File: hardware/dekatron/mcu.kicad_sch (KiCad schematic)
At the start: 30 parts, among them J301 DISP, J302 NIX_LV, U301 RP2040-Zero

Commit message: Tie the dekatron cathodes at the socket; add Phase 1C PCB tooling (WIP)
Cathodes K0, K2-K9 are joined at the socket and return on one RTN wire, as
in the AD01 reference: LK6-LK14 and J203 removed, tube harness is anode
(J201) + G1, G2, K1, RTN (J202, 4 pads). Netlist diff: only the nine
TUBE_Kn nets and the RTN link pins change. ERC 1 (intentional).

Also adds work-in-progress PCB tooling: gen_pcb.py (pcbnew placement,
outline, pours, rules), route_pcb.py (class-aware A* router adapted from
nanovolt-divider), pcb_io.py, and dekatron.kicad_dru with the corrected
HV pair rules (HV to HV/VB/HVSTR 1.5 mm, to bias/logic 3.0 mm). Harness
landings use plain wire pads with cable-tie anchors. The board itself is
not committed yet: placement is being reworked.

Co-Authored-By: Claude Opus 5.5 <noreply@anthropic.com>
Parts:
- J301: footprint Connector_Wire:SolderWire-0.5sqmm_1x05_P4.8mm_D0.9mm_OD2.3mm_Relief -> Connector_Wire:SolderWire-0.5sqmm_1x05_P4.8mm_D0.9mm_OD2.3mm
- J302: footprint Connector_Wire:SolderWire-0.5sqmm_1x06_P4.8mm_D0.9mm_OD2.3mm_Relief -> Connector_Wire:SolderWire-0.5sqmm_1x06_P4.8mm_D0.9mm_OD2.3mm
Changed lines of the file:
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@@
 	  (property "Reference" "J301" (at 153.06 242.84 0) (show_name no) (do_not_autoplace no) (effects (font (size 1.27 1.27)) (justify left)))
 	  (property "Value" "DISP" (at 153.06 245.44 0) (show_name no) (do_not_autoplace no) (effects (font (size 1.27 1.27)) (justify left)))
-	  (property "Footprint" "Connector_Wire:SolderWire-0.5sqmm_1x05_P4.8mm_D0.9mm_OD2.3mm_Relief" (at 149.86 243.84 0) (hide yes) (show_name no) (do_not_autoplace no) (effects (font (size 1.27 1.27)) (justify left)))
+	  (property "Footprint" "Connector_Wire:SolderWire-0.5sqmm_1x05_P4.8mm_D0.9mm_OD2.3mm" (at 149.86 243.84 0) (hide yes) (show_name no) (do_not_autoplace no) (effects (font (size 1.27 1.27)) (justify left)))
 	  (property "Datasheet" "" (at 149.86 243.84 0) (hide yes) (show_name no) (do_not_autoplace no) (effects (font (size 1.27 1.27)) (justify left)))
 	  (property "Description" "Generic connector, single row, 01x05, script generated (kicad-library-utils/schlib/autogen/connector/)" (at 149.86 243.84 0) (hide yes) (show_name no) (do_not_autoplace no) (effects (font (size 1.27 1.27)) (justify left)))
@@
 	  (property "Reference" "J302" (at 214.02 242.84 0) (show_name no) (do_not_autoplace no) (effects (font (size 1.27 1.27)) (justify left)))
 	  (property "Value" "NIX_LV" (at 214.02 245.44 0) (show_name no) (do_not_autoplace no) (effects (font (size 1.27 1.27)) (justify left)))
-	  (property "Footprint" "Connector_Wire:SolderWire-0.5sqmm_1x06_P4.8mm_D0.9mm_OD2.3mm_Relief" (at 210.82 243.84 0) (hide yes) (show_name no) (do_not_autoplace no) (effects (font (size 1.27 1.27)) (justify left)))
+	  (property "Footprint" "Connector_Wire:SolderWire-0.5sqmm_1x06_P4.8mm_D0.9mm_OD2.3mm" (at 210.82 243.84 0) (hide yes) (show_name no) (do_not_autoplace no) (effects (font (size 1.27 1.27)) (justify left)))
 	  (property "Datasheet" "" (at 210.82 243.84 0) (hide yes) (show_name no) (do_not_autoplace no) (effects (font (size 1.27 1.27)) (justify left)))
 	  (property "Description" "Generic connector, single row, 01x06, script generated (kicad-library-utils/schlib/autogen/connector/)" (at 210.82 243.84 0) (hide yes) (show_name no) (do_not_autoplace no) (effects (font (size 1.27 1.27)) (justify left)))

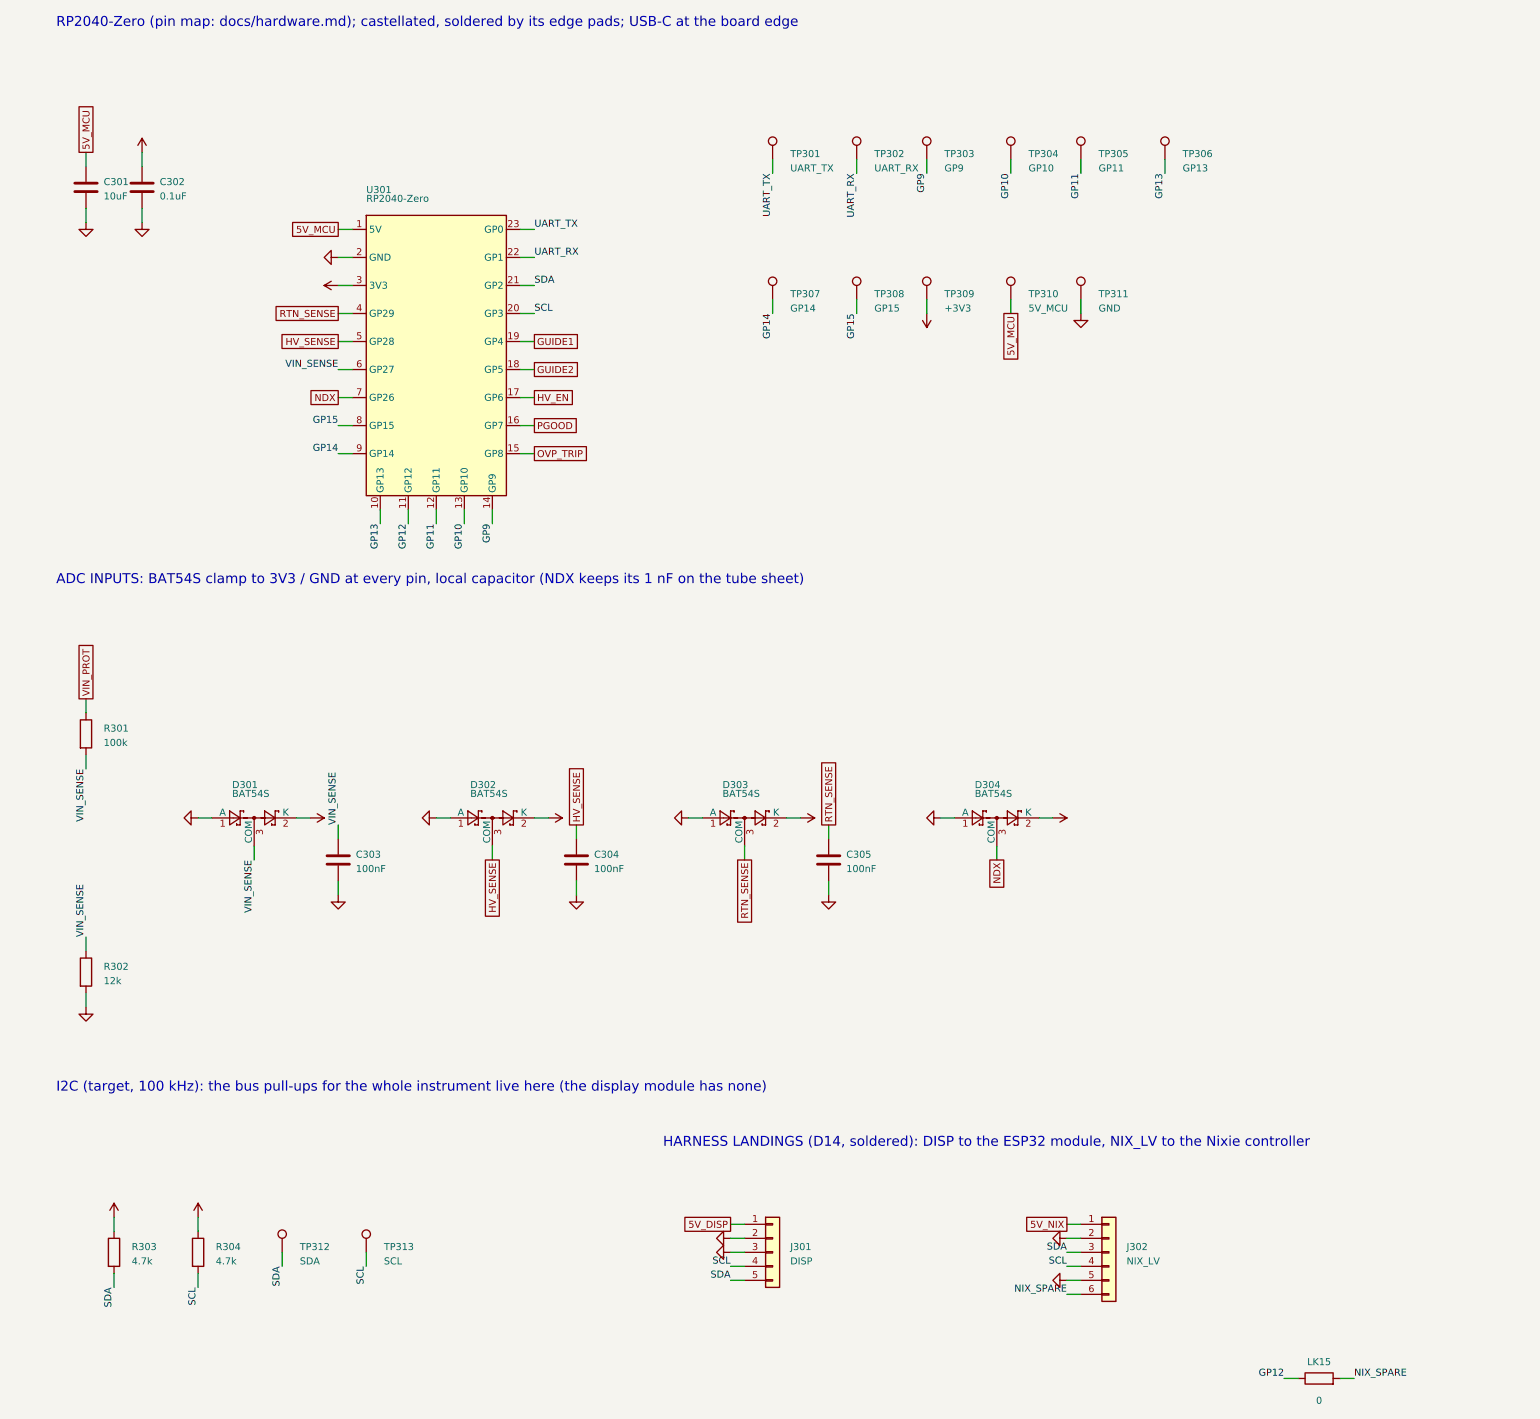
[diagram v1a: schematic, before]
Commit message: Redraw the dekatron schematics as wired, readable sheets
Each block is now drawn with real wires, power/GND symbols and junctions
instead of per-pin label stubs. Net names used by the PCB scripts and net
classes are kept as local labels; inter-sheet nets stay global labels.
Netlist pin partition verified identical to the previous version; ERC
unchanged (1 intentional LP2951/LM5156 power-output violation).

Co-Authored-By: Claude Opus 5.5 <noreply@anthropic.com>
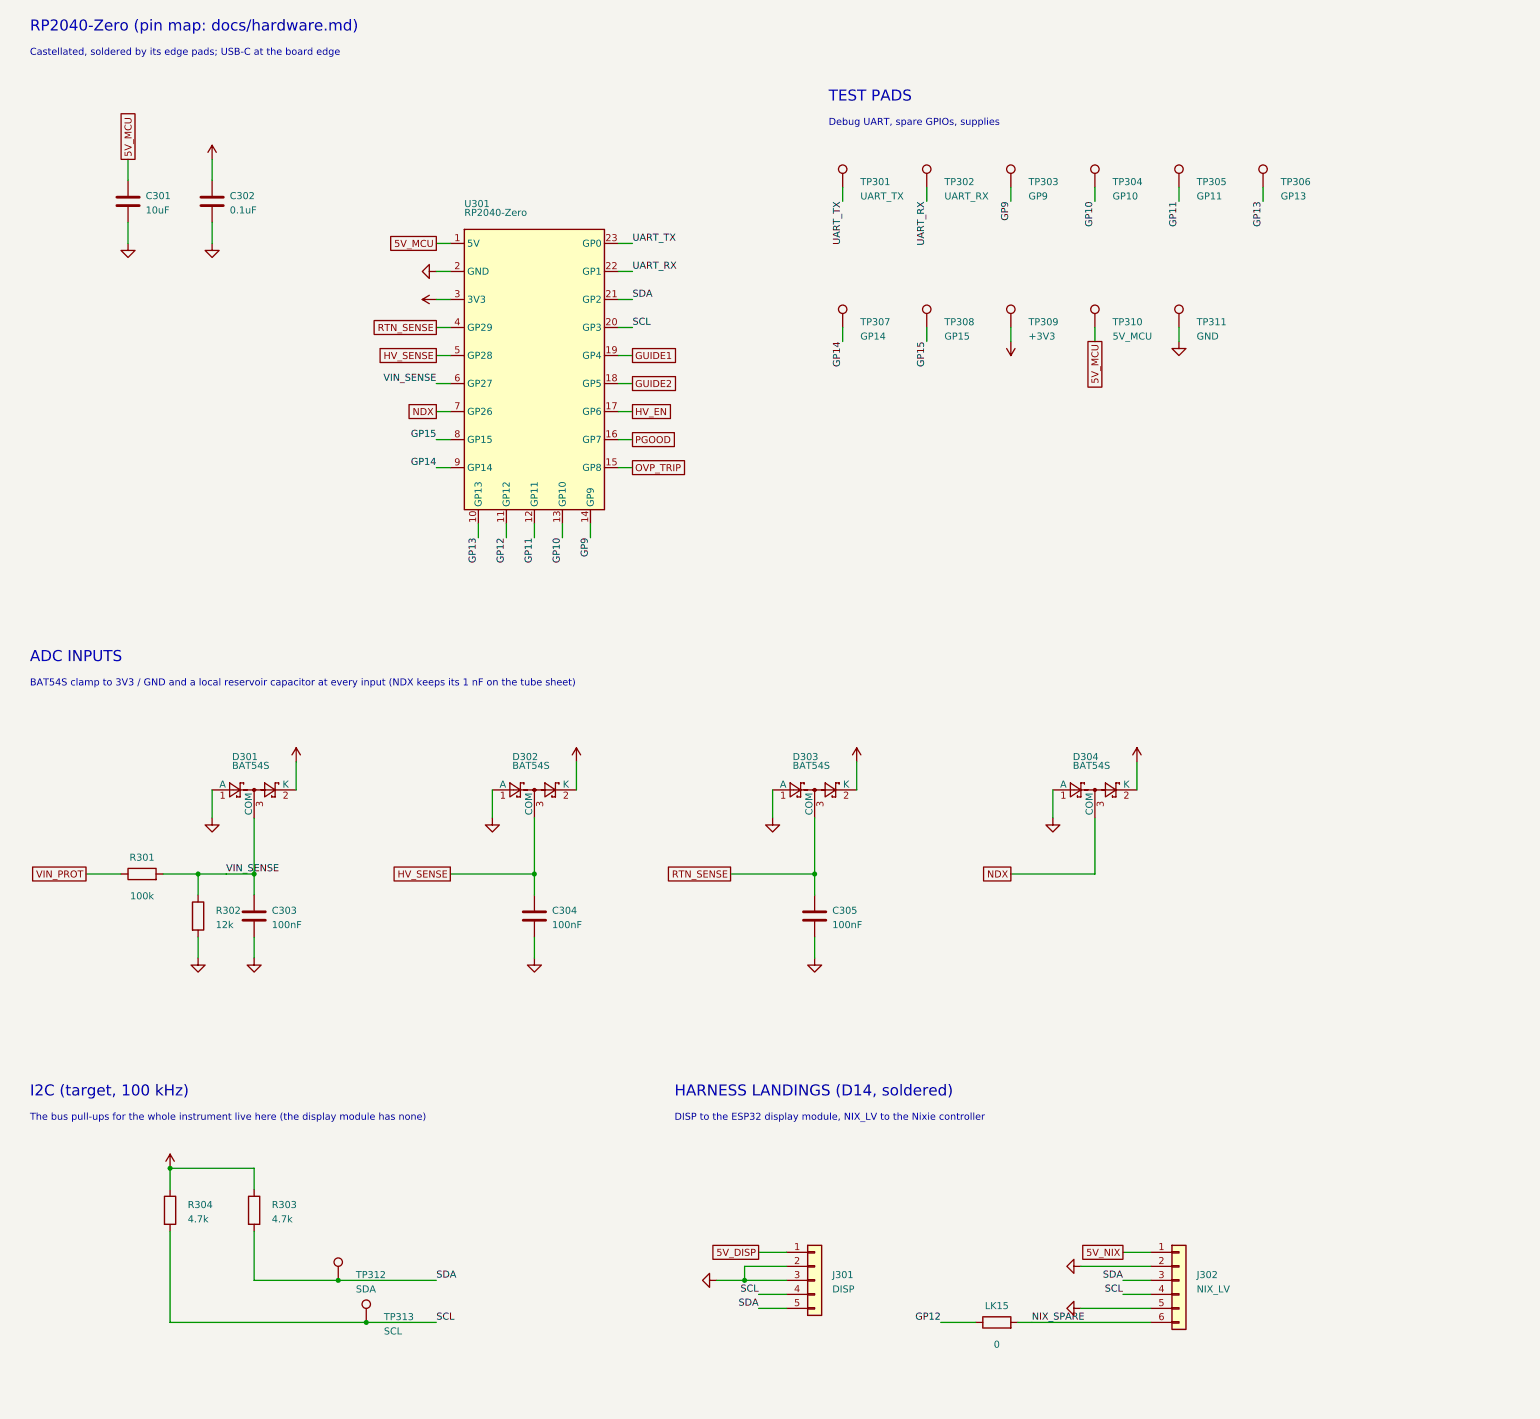
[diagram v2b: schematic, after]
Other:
- note added: "ADC INPUTS"
- note added: "BAT54S clamp to 3V3 / GND and a local reservoir capacitor at every input (NDX keeps its 1 nF on the tube sheet)"
- note added: "Castellated, soldered by its edge pads; USB-C at the board edge"
- note added: "DISP to the ESP32 display module, NIX_LV to the Nixie controller"
- note added: "Debug UART, spare GPIOs, supplies"
- note added: "HARNESS LANDINGS (D14, soldered)"
- note added: "I2C (target, 100 kHz)"
- note added: "RP2040-Zero (pin map: docs/hardware.md)"
- note added: "TEST PADS"
- note added: "The bus pull-ups for the whole instrument live here (the display module has none)"
- note removed: "ADC INPUTS: BAT54S clamp to 3V3 / GND at every pin, local capacitor (NDX keeps its 1 nF on the tube sheet)"
- note removed: "HARNESS LANDINGS (D14, soldered): DISP to the ESP32 module, NIX_LV to the Nixie controller"
- note removed: "I2C (target, 100 kHz): the bus pull-ups for the whole instrument live here (the display module has none)"
- note removed: "RP2040-Zero (pin map: docs/hardware.md); castellated, soldered by its edge pads; USB-C at the board edge"
- moved on the sheet: R304

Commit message: Replace 1206 HV resistor strings with single leaded HVR25/HVR37 parts
- Drop the dedicated HV bleeder; the feedback divider (HVR25 4.75M/10.5k,
  453.4 V) and a shared monitor/OVP divider (HVR25 4.64M/14.0k/10.5k,
  OVP 551.8 V, HV_SENSE = HV/190.4) discharge HV: <50 V in 1.94 s,
  3.9 s with one divider open (hv_discharge.cir).
- Dummy load: one DNP HVR37 910k. V_b bleeder/OVP, RTN_SENSE, index
  divider: single HVR25. Anode: 2 x HVR37 332k. G+/RTN feed: MRS25 40.2k.
- C304 (HV_SENSE) 100 nF -> 10 nF: on a feedback-open runaway the shared
  OVP tap lagged HV by 15.8 V with 100 nF (fault_fbopen.cir).
- BOM 180 -> 155 parts; ERC unchanged.

Co-Authored-By: Claude Opus 5.5 <noreply@anthropic.com>
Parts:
- C304: value 100nF -> 10nF
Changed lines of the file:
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@@
 	(symbol (lib_id "Device:C") (at 106.68 182.88 0) (unit 1) (body_style 1) (exclude_from_sim no) (in_bom yes) (on_board yes) (in_pos_files yes) (dnp no)
 	  (property "Reference" "C304" (at 109.88 181.88 0) (show_name no) (do_not_autoplace no) (effects (font (size 1.27 1.27)) (justify left)))
-	  (property "Value" "100nF" (at 109.88 184.48 0) (show_name no) (do_not_autoplace no) (effects (font (size 1.27 1.27)) (justify left)))
+	  (property "Value" "10nF" (at 109.88 184.48 0) (show_name no) (do_not_autoplace no) (effects (font (size 1.27 1.27)) (justify left)))
 	  (property "Footprint" "Capacitor_SMD:C_1206_3216Metric" (at 106.68 182.88 0) (hide yes) (show_name no) (do_not_autoplace no) (effects (font (size 1.27 1.27)) (justify left)))
 	  (property "Datasheet" "" (at 106.68 182.88 0) (hide yes) (show_name no) (do_not_autoplace no) (effects (font (size 1.27 1.27)) (justify left)))
